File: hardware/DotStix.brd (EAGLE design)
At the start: 20.3 x 50 mm, 29 parts, among them IC2 SI1145, U1 ATMEGA328P-MU-QFN32, U2 TMP102, U4 9DoF IMU

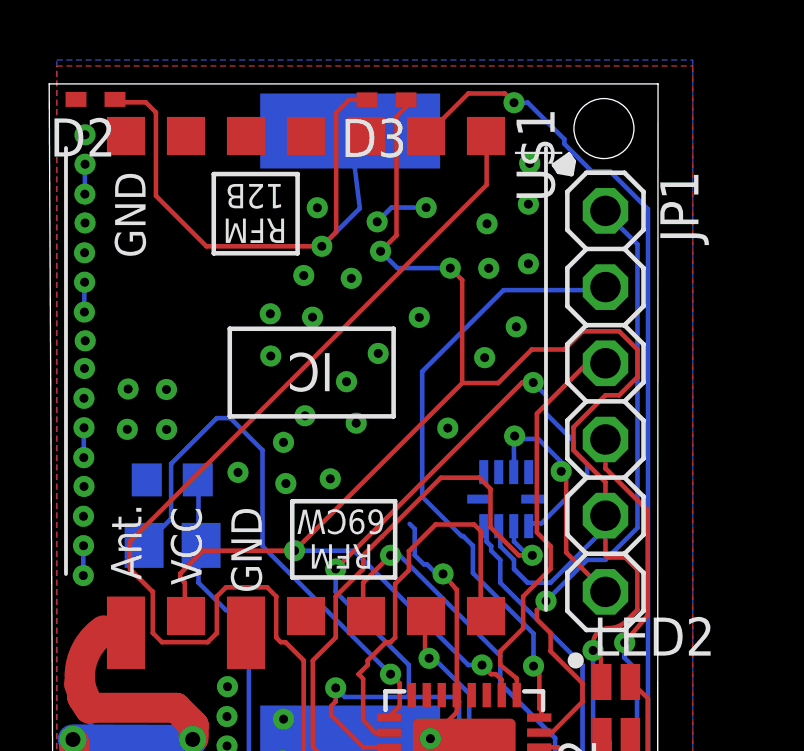
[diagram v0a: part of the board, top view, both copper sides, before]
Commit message: Add 256kb EEPROM
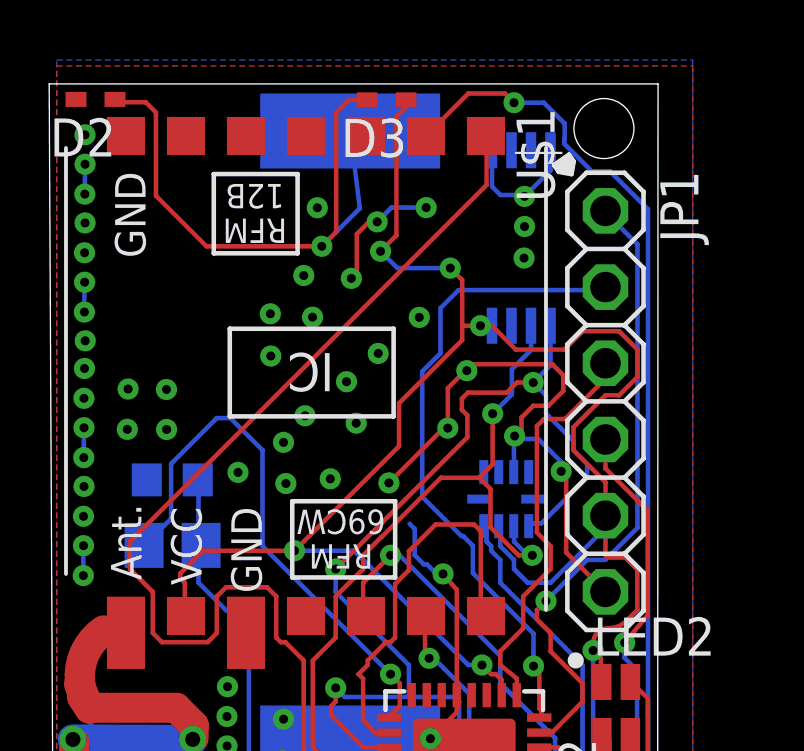
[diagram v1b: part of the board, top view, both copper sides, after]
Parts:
- added IC1: CAT24M010TS, CAT24M01YI:TSSOP8
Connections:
- net +3V3: now also IC1.VCC
- net GND: now also IC1.GND, IC1.NC
- net SCL: now also IC1.SCL
- net SDA: now also IC1.SDA
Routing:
- net GND: track 78.0 -> 96.1 mm, vias 110 -> 108
- net SCL: track 37.6 -> 43.4 mm, vias 3 -> 4
- net SDA: track 53.7 -> 56.9 mm
- net MISO: track 20.6 -> 21.5 mm
- net SCK: track 13.5 -> 14.2 mm
- net +3V3: track 160.9 -> 161.1 mm, vias 9 -> 10

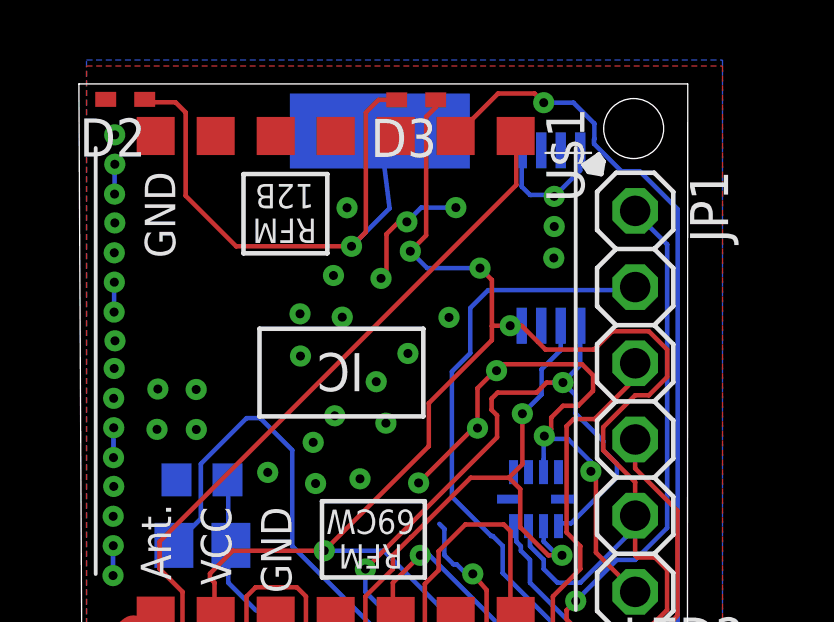
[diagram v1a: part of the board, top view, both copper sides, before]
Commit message: Add reed switch for RST. Required for potting
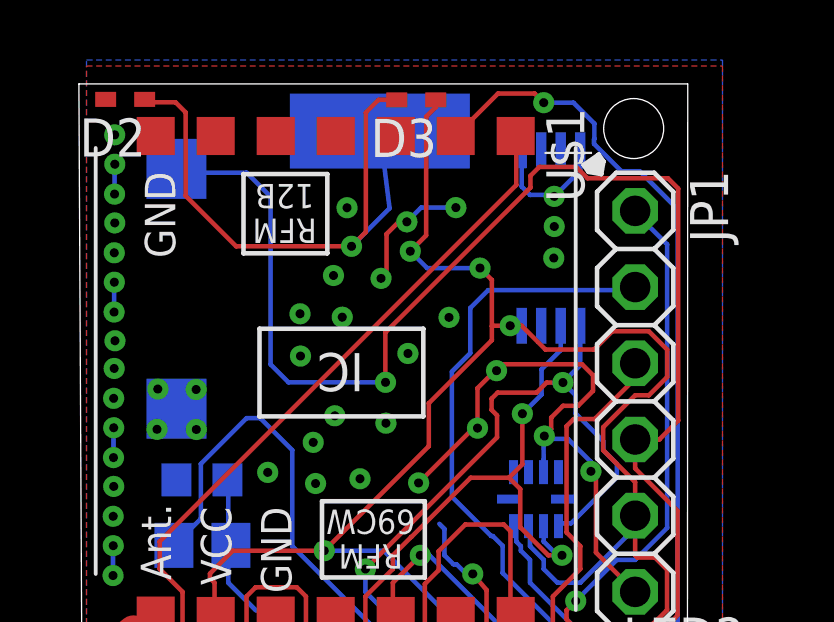
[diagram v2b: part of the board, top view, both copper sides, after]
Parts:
- added TP5, TP6: TPTP20SQ, testpad:TP20SQ
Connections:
- net GND: now also TP5.TP
- net RST: now also TP6.TP
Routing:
- net RST: track 78.7 -> 115.6 mm, vias 6 -> 7
- net GND: vias 108 -> 107
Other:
- board text added: "DotStix v0.4.1"
- board text removed: "DotStix v0.3.1"
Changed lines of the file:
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@@
 <grid distance="0.00254" unitdist="mm" unit="mm" style="lines" multiple="1" display="yes" altdistance="0.025" altunitdist="inch" altunit="inch"/>
 <layers>
-<layer number="1" name="Top" color="4" fill="1" visible="yes" active="yes"/>
-<layer number="16" name="Bottom" color="1" fill="1" visible="yes" active="yes"/>
-<layer number="17" name="Pads" color="2" fill="1" visible="yes" active="yes"/>
-<layer number="18" name="Vias" color="2" fill="1" visible="yes" active="yes"/>
-<layer number="19" name="Unrouted" color="6" fill="1" visible="yes" active="yes"/>
-<layer number="20" name="Dimension" color="15" fill="1" visible="yes" active="yes"/>
-<layer number="21" name="tPlace" color="7" fill="1" visible="yes" active="yes"/>
+<layer number="1" name="Top" color="4" fill="1" visible="no" active="yes"/>
+<layer number="16" name="Bottom" color="1" fill="1" visible="no" active="yes"/>
+<layer number="17" name="Pads" color="2" fill="1" visible="no" active="yes"/>
+<layer number="18" name="Vias" color="2" fill="1" visible="no" active="yes"/>
+<layer number="19" name="Unrouted" color="6" fill="1" visible="no" active="yes"/>
+<layer number="20" name="Dimension" color="15" fill="1" visible="no" active="yes"/>
+<layer number="21" name="tPlace" color="7" fill="1" visible="no" active="yes"/>
 <layer number="22" name="bPlace" color="7" fill="1" visible="yes" active="yes"/>
-<layer number="23" name="tOrigins" color="15" fill="1" visible="yes" active="yes"/>
-<layer number="24" name="bOrigins" color="15" fill="1" visible="yes" active="yes"/>
+<layer number="23" name="tOrigins" color="15" fill="1" visible="no" active="yes"/>
+<layer number="24" name="bOrigins" color="15" fill="1" visible="no" active="yes"/>
 <layer number="25" name="tNames" color="7" fill="1" visible="no" active="yes"/>
 <layer number="26" name="bNames" color="7" fill="1" visible="no" active="yes"/>
@@
 <layer number="46" name="Milling" color="3" fill="1" visible="no" active="yes"/>
 <layer number="47" name="Measures" color="7" fill="1" visible="no" active="yes"/>
-<layer number="48" name="Document" color="7" fill="1" visible="yes" active="yes"/>
+<layer number="48" name="Document" color="7" fill="1" visible="no" active="yes"/>
 <layer number="49" name="Reference" color="7" fill="1" visible="no" active="yes"/>
 <layer number="50" name="dxf" color="7" fill="1" visible="no" active="no"/>
@@
 <rectangle x1="9.1059" y1="9.8679" x2="9.7917" y2="9.8933" layer="22" rot="R180"/>
 <rectangle x1="7.4803" y1="9.8679" x2="8.6487" y2="9.8933" layer="22" rot="R180"/>
-<text x="4.7650375" y="44.0436" size="1.27" layer="22" rot="MR270" align="center">Mihai Galos</text>
-<text x="9.6774" y="11.4046" size="1.016" layer="22" rot="MR0" align="center">DotStix v0.3.1</text>
+<text x="4.983478125" y="43.2206375" size="1.27" layer="22" rot="MR270" align="center">Mihai Galos</text>
+<text x="9.6774" y="11.4046" size="1.016" layer="22" rot="MR0" align="center">DotStix v0.4.1</text>
 <circle x="17.2974" y="30.7848" radius="0.193440625" width="0.1524" layer="21"/>
 <circle x="17.27961875" y="30.7848" radius="0.071840625" width="0.1524" layer="21"/>
@@
 <dimension x1="19.99" y1="50.0026" x2="20.0916" y2="0" x3="35.939746875" y3="25.033603125" textsize="1.778" layer="47"/>
 <dimension x1="0" y1="0" x2="20.0154" y2="0" x3="10.0077" y3="-3.2766" textsize="1.778" layer="47"/>
-<text x="3.0226" y="44.0436" size="1.016" layer="22" rot="MR270" align="center">01/2018</text>
+<text x="2.481578125" y="21.714459375" size="1.016" layer="22" rot="SMR270" align="center">01/2018</text>
 <text x="2.489203125" y="17.579340625" size="1.016" layer="21" rot="SR90" align="center">HexID</text>
 <rectangle x1="1.320803125" y1="20.500340625" x2="3.759203125" y2="24.919940625" layer="21"/>
@@
 <attribute name="MPN" value="24C00T-E/ST" x="16.751303125" y="49.049940625" size="1.778" layer="28" rot="MR270" display="off"/>
 </element>
+<element name="TP5" library="testpad" package="TP20SQ" value="TPTP20SQ" x="2.999740625" y="39.176959375" rot="MR0">
+<attribute name="TP_SIGNAL_NAME" value="" x="2.999740625" y="39.176959375" size="1.778" layer="28" rot="MR0" display="off"/>
+</element>
+<element name="TP6" library="testpad" package="TP20SQ" value="TPTP20SQ" x="2.997203125" y="47.1703375" rot="MR0">
+<attribute name="TP_SIGNAL_NAME" value="" x="2.997203125" y="47.1703375" size="1.778" layer="28" rot="MR0" display="off"/>
+</element>
 </elements>
 <signals>
@@
 <wire x1="11.153134375" y1="45.88001875" x2="12.311378125" y2="45.88001875" width="0.1524" layer="16"/>
 <via x="10.71371875" y="41.018459375" extent="1-16" drill="0.3"/>
-<via x="9.657078125" y="40.07611875" extent="1-16" drill="0.3"/>
 <via x="8.27531875" y="38.940740625" extent="1-16" drill="0.3"/>
 <via x="7.556496875" y="38.05428125" extent="1-16" drill="0.3"/>
@@
 <wire x1="9.99998125" y1="44.998640625" x2="9.99998125" y2="43.703240625" width="0.1524" layer="1"/>
 <wire x1="9.99998125" y1="43.703240625" x2="9.8171" y2="43.520359375" width="0.1524" layer="1"/>
+<via x="13.6677375" y="40.44441875" extent="1-16" drill="0.3"/>
+<contactref element="TP5" pad="TP"/>
 <wire x1="5.67181875" y1="28.915359375" x2="5.6896" y2="29.911040625" width="0" layer="19" extent="1-1"/>
 <wire x1="5.65911875" y1="24.003" x2="5.656578125" y2="24.983440625" width="0" layer="19" extent="1-1"/>
-<via x="13.6677375" y="40.44441875" extent="1-16" drill="0.3"/>
 </signal>
 <signal name="SDA">
@@
 <wire x1="17.2974" y1="20.5359" x2="17.2974" y2="18.0594" width="0.1524" layer="1"/>
 <wire x1="17.2974" y1="18.0594" x2="17.526" y2="17.8308" width="0.1524" layer="1"/>
+<contactref element="TP6" pad="TP"/>
+<wire x1="18.288" y1="38.1508" x2="19.09571875" y2="38.1508" width="0.1524" layer="1"/>
+<wire x1="19.09571875" y1="38.1508" x2="19.7231" y2="38.77818125" width="0.1524" layer="1"/>
+<wire x1="19.7231" y1="38.77818125" x2="19.7231" y2="46.51501875" width="0.1524" layer="1"/>
+<wire x1="19.7231" y1="46.51501875" x2="19.3802" y2="46.85791875" width="0.1524" layer="1"/>
+<wire x1="19.3802" y1="46.85791875" x2="16.700503125" y2="46.85791875" width="0.1524" layer="1"/>
+<wire x1="16.700503125" y1="46.85791875" x2="16.322040625" y2="47.23638125" width="0.1524" layer="1"/>
+<wire x1="16.322040625" y1="47.23638125" x2="15.095221875" y2="47.23638125" width="0.1524" layer="1"/>
+<wire x1="15.095221875" y1="47.23638125" x2="14.798040625" y2="46.9392" width="0.1524" layer="1"/>
+<wire x1="14.798040625" y1="46.9392" x2="14.798040625" y2="46.548040625" width="0.1524" layer="1"/>
+<wire x1="14.798040625" y1="46.548040625" x2="9.96188125" y2="41.7169625" width="0.1524" layer="1"/>
+<wire x1="9.96188125" y1="41.7169625" x2="9.96188125" y2="40.060878125" width="0.1524" layer="1"/>
+<wire x1="9.96188125" y1="40.060878125" x2="9.966959375" y2="40.0558" width="0.1524" layer="1"/>
+<via x="9.966959375" y="40.0558" extent="1-16" drill="0.3"/>
+<wire x1="9.966959375" y1="40.0558" x2="6.733540625" y2="40.0558" width="0.1524" layer="16"/>
+<wire x1="6.733540625" y1="40.0558" x2="6.1341" y2="40.655240625" width="0.1524" layer="16"/>
+<wire x1="6.1341" y1="40.655240625" x2="6.1341" y2="46.248321875" width="0.1524" layer="16"/>
+<wire x1="6.1341" y1="46.248321875" x2="5.33908125" y2="47.043340625" width="0.1524" layer="16"/>
+<wire x1="5.33908125" y1="47.043340625" x2="3.1242" y2="47.043340625" width="0.1524" layer="16"/>
+<wire x1="3.1242" y1="47.043340625" x2="2.997203125" y2="47.1703375" width="0.1524" layer="16"/>
 </signal>
 <signal name="RSEL">

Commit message: Increment version, rearrange text
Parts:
- moved R4 0.68 mm to (3.83, 36.1)
- moved R3 0.60 mm to (3.86, 34.0)
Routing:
- net LIGHT_SENSE: track 17.8 -> 19.4 mm
- net LIGHT_SENSE_ENA: track 18.2 -> 18.7 mm
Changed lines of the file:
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@@
 <grid distance="0.00254" unitdist="mm" unit="mm" style="lines" multiple="1" display="yes" altdistance="0.025" altunitdist="inch" altunit="inch"/>
 <layers>
-<layer number="1" name="Top" color="4" fill="1" visible="no" active="yes"/>
-<layer number="16" name="Bottom" color="1" fill="1" visible="no" active="yes"/>
-<layer number="17" name="Pads" color="2" fill="1" visible="no" active="yes"/>
-<layer number="18" name="Vias" color="2" fill="1" visible="no" active="yes"/>
-<layer number="19" name="Unrouted" color="6" fill="1" visible="no" active="yes"/>
-<layer number="20" name="Dimension" color="15" fill="1" visible="no" active="yes"/>
-<layer number="21" name="tPlace" color="7" fill="1" visible="no" active="yes"/>
+<layer number="1" name="Top" color="4" fill="1" visible="yes" active="yes"/>
+<layer number="16" name="Bottom" color="1" fill="1" visible="yes" active="yes"/>
+<layer number="17" name="Pads" color="2" fill="1" visible="yes" active="yes"/>
+<layer number="18" name="Vias" color="2" fill="1" visible="yes" active="yes"/>
+<layer number="19" name="Unrouted" color="6" fill="1" visible="yes" active="yes"/>
+<layer number="20" name="Dimension" color="15" fill="1" visible="yes" active="yes"/>
+<layer number="21" name="tPlace" color="7" fill="1" visible="yes" active="yes"/>
 <layer number="22" name="bPlace" color="7" fill="1" visible="yes" active="yes"/>
-<layer number="23" name="tOrigins" color="15" fill="1" visible="no" active="yes"/>
-<layer number="24" name="bOrigins" color="15" fill="1" visible="no" active="yes"/>
+<layer number="23" name="tOrigins" color="15" fill="1" visible="yes" active="yes"/>
+<layer number="24" name="bOrigins" color="15" fill="1" visible="yes" active="yes"/>
 <layer number="25" name="tNames" color="7" fill="1" visible="no" active="yes"/>
 <layer number="26" name="bNames" color="7" fill="1" visible="no" active="yes"/>
@@
 <dimension x1="19.99" y1="50.0026" x2="20.0916" y2="0" x3="35.939746875" y3="25.033603125" textsize="1.778" layer="47"/>
 <dimension x1="0" y1="0" x2="20.0154" y2="0" x3="10.0077" y3="-3.2766" textsize="1.778" layer="47"/>
-<text x="2.481578125" y="21.714459375" size="1.016" layer="22" rot="SMR270" align="center">01/2018</text>
+<text x="2.557784375" y="21.775421875" size="1.016" layer="22" rot="SMR90" align="center">01/2018</text>
 <text x="2.489203125" y="17.579340625" size="1.016" layer="21" rot="SR90" align="center">HexID</text>
 <rectangle x1="1.320803125" y1="20.500340625" x2="3.759203125" y2="24.919940625" layer="21"/>
@@
 <attribute name="TP_SIGNAL_NAME" value="" x="14.3002" y="2.2352" size="1.016" layer="28" rot="MR270" display="off"/>
 </element>
-<element name="R3" library="resistor" package="R0805" value="" x="3.8608" y="34.6202" rot="MR0"/>
-<element name="R4" library="resistor" package="R0603" value="10kΩ" x="3.8481" y="36.8046" rot="MR180"/>
+<element name="R3" library="resistor" package="R0805" value="" x="3.8608" y="34.020759375" rot="MR0"/>
+<element name="R4" library="resistor" package="R0603" value="10kΩ" x="3.83031875" y="36.12388125" rot="MR180"/>
 <element name="Y1" library="SparkFun-Clocks" package="RESONATOR-SMD-3.2X1.3" value="" x="15.542259375" y="21.79574375" rot="R180"/>
 <element name="Y2" library="SparkFun-Clocks" package="CRYSTAL-SMD-3.2X1.5MM" value="" x="15.4914625" y="21.800821875" rot="R180"/>
@@
 <wire x1="4.7244" y1="34.5948" x2="4.7244" y2="33.3756" width="0.1524" layer="16"/>
 <wire x1="11.8872" y1="24.5364" x2="11.831378125" y2="24.629740625" width="0.1524" layer="1"/>
-<wire x1="4.7244" y1="34.5948" x2="4.8108" y2="34.6202" width="0.1524" layer="16"/>
+<wire x1="4.7244" y1="34.5948" x2="4.8108" y2="34.020759375" width="0.1524" layer="16"/>
 <wire x1="4.7244" y1="34.7472" x2="4.7244" y2="36.7284" width="0.1524" layer="16"/>
-<wire x1="4.7244" y1="36.7284" x2="4.6981" y2="36.8046" width="0.1524" layer="16"/>
-<wire x1="4.7244" y1="34.7472" x2="4.8108" y2="34.6202" width="0.1524" layer="16"/>
+<wire x1="4.7244" y1="36.7284" x2="4.68031875" y2="36.12388125" width="0.1524" layer="16"/>
+<wire x1="4.7244" y1="34.7472" x2="4.8108" y2="34.020759375" width="0.1524" layer="16"/>
 <via x="8.6868" y="25.2984" extent="1-16" drill="0.3"/>
 <wire x1="11.03058125" y1="24.629740625" x2="11.831378125" y2="24.629740625" width="0.1524" layer="1"/>
@@
 <wire x1="3.048" y1="34.7472" x2="3.81" y2="35.5092" width="0.1524" layer="16"/>
 <wire x1="11.1252" y1="28.956" x2="11.081378125" y2="28.879740625" width="0.1524" layer="1"/>
-<wire x1="3.048" y1="34.7472" x2="2.9108" y2="34.6202" width="0.1524" layer="16"/>
+<wire x1="3.048" y1="34.7472" x2="2.9108" y2="34.020759375" width="0.1524" layer="16"/>
 <via x="11.1252" y="30.3276" extent="1-16" drill="0.3"/>
 </signal>

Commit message: Modify pullup value for reed, add explanation
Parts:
- R5: value >1MΩ -> 470kΩ
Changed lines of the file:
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@@
 <layer number="46" name="Milling" color="3" fill="1" visible="no" active="yes"/>
 <layer number="47" name="Measures" color="7" fill="1" visible="no" active="yes"/>
-<layer number="48" name="Document" color="7" fill="1" visible="no" active="yes"/>
+<layer number="48" name="Document" color="7" fill="1" visible="yes" active="yes"/>
 <layer number="49" name="Reference" color="7" fill="1" visible="no" active="yes"/>
 <layer number="50" name="dxf" color="7" fill="1" visible="no" active="no"/>
@@
 <element name="C7" library="rcl" package="C0603" value="7pF" x="16.461740625" y="18.752821875" rot="R270"/>
 <element name="C9" library="rcl" package="C0603" value="7pF" x="14.452603125" y="18.7833" rot="R270"/>
-<element name="R5" library="resistor" package="R0603" value="&gt;1MΩ" x="16.5633375" y="15.10538125" rot="R270"/>
+<element name="R5" library="resistor" package="R0603" value="470kΩ" x="16.5633375" y="15.10538125" rot="R270"/>
 <element name="C6" library="adafruit" package="C3216" value="100uF 4V" x="7.406640625" y="19.2684375" rot="R90"/>
 <element name="SJ1" library="SparkFun" package="SJ_2S-TRACE" value="SOLDERJUMPERTRACE" x="7.27201875" y="23.395940625" rot="MR0"/>
